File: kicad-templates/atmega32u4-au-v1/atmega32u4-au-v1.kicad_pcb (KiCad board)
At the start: 2 copper layers, 17 parts, among them P1 USB_C_Plug_USB2.0, U1 ATMEGA32U4-AU, U2 TPD2S017, Y1 16MHz

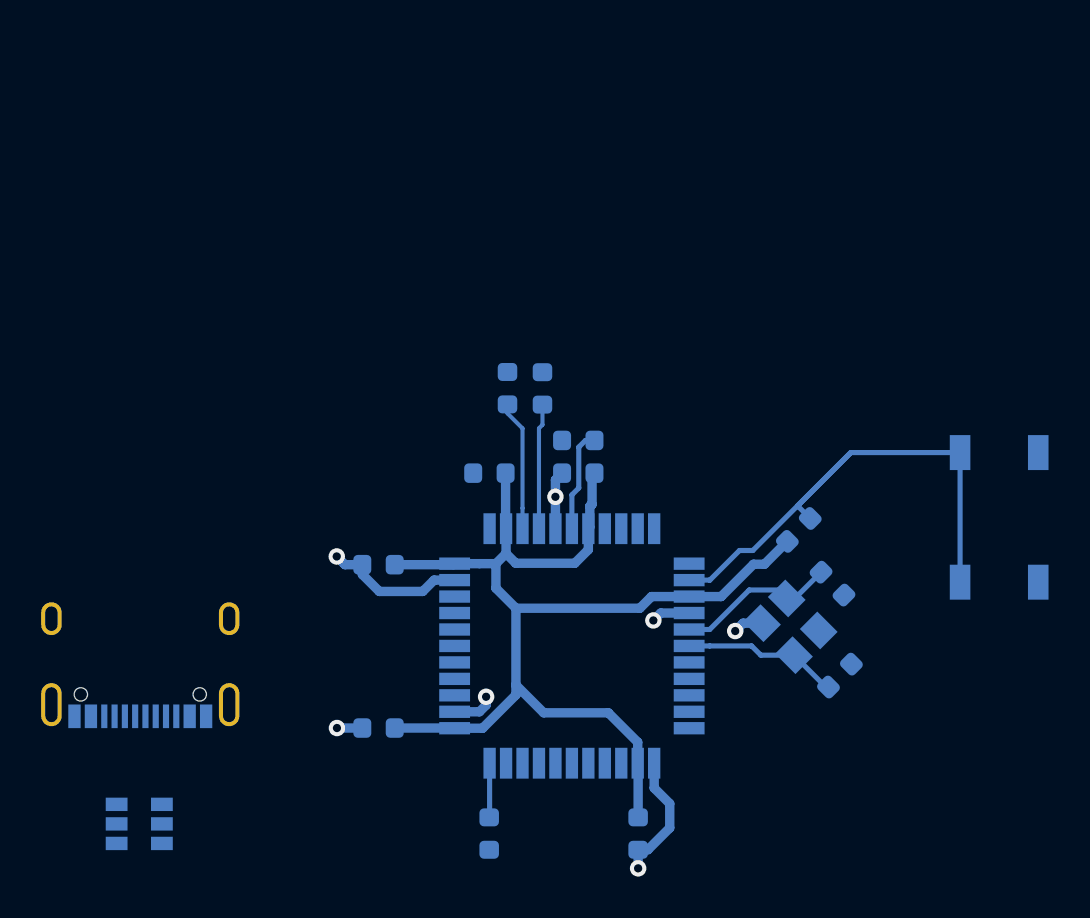
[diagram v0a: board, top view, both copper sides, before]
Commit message: change USB-C plug to receptacle, update template
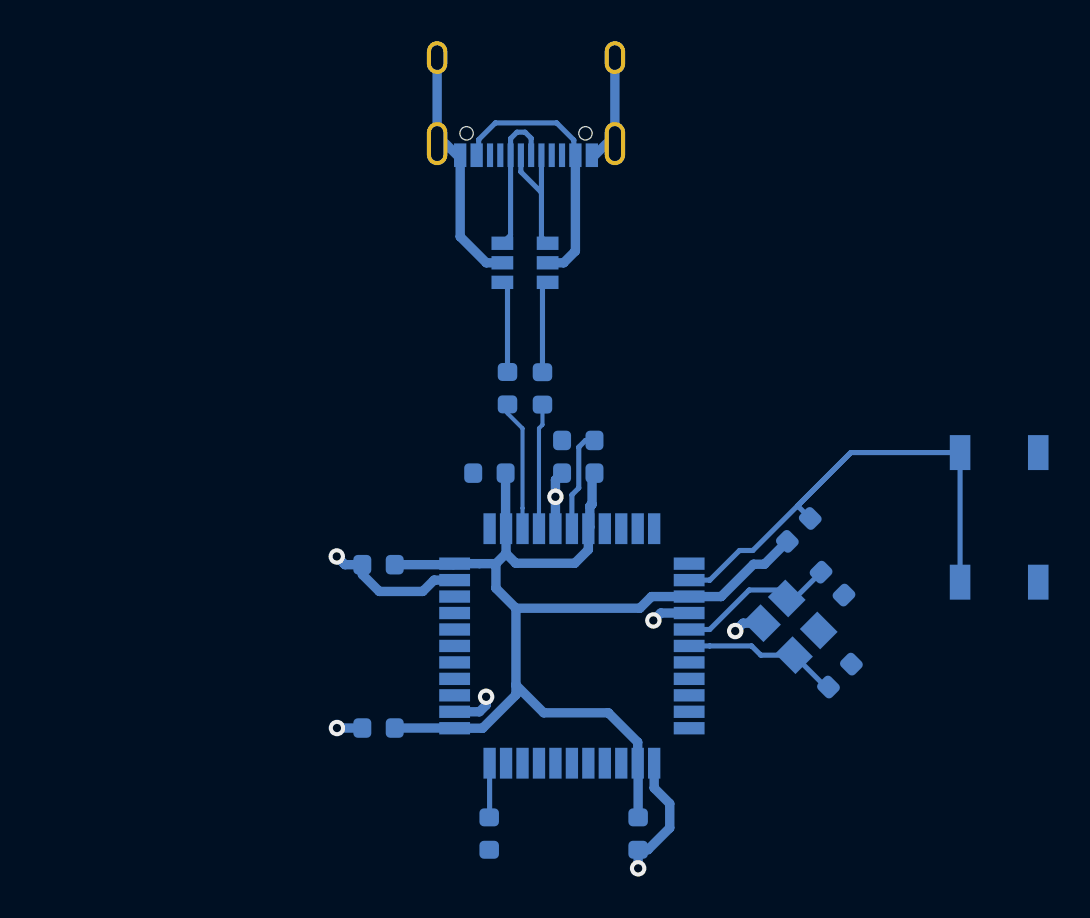
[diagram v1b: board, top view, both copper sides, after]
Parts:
- J1: renamed from P1; value USB_C_Plug_USB2.0 -> USB_C_Receptacle_USB2.0
- U1: value ATMEGA32U4-AU -> ATmega16U4-AU
- Y1: value 16MHz -> Crystal_GND24
- moved J1 33.1 mm to (18.8, -27.3)
- moved U2 33.1 mm to (18.7, -18.4)
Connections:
- C1 pad 1: (no net) -> N$1
- C1 pad 2: (no net) -> GND
- C2 pad 1: (no net) -> N$2
- C2 pad 2: (no net) -> GND
- C3 pad 1: (no net) -> VCC
- C3 pad 2: (no net) -> GND
- C4 pad 1: (no net) -> VCC
- C4 pad 2: (no net) -> GND
- C5 pad 1: (no net) -> VCC
- C5 pad 2: (no net) -> GND
- C6 pad 1: (no net) -> VCC
- C6 pad 2: (no net) -> GND
- C7 pad 1: (no net) -> VCC
- C7 pad 2: (no net) -> GND
- C8 pad 1: (no net) -> N$3
- C8 pad 2: (no net) -> GND
- J1 pad A1: (no net) -> GND
- J1 pad A12: (no net) -> GND
- J1 pad A4: (no net) -> VCC
- J1 pad A6: (no net) -> N$5
- J1 pad A7: (no net) -> N$4
- J1 pad A9: (no net) -> VCC
- J1 pad B1: (no net) -> GND
- J1 pad B12: (no net) -> GND
- J1 pad B4: (no net) -> VCC
- J1 pad B6: (no net) -> N$5
- J1 pad B7: (no net) -> N$4
- J1 pad B9: (no net) -> VCC
- J1 pad S1: (no net) -> GND
- R1 pad 1: (no net) -> N$8
- R1 pad 2: (no net) -> N$6
- R2 pad 1: (no net) -> N$9
- R2 pad 2: (no net) -> N$7
- R3 pad 1: (no net) -> N$10
- R3 pad 2: (no net) -> GND
- R4 pad 1: (no net) -> N$11
- R4 pad 2: (no net) -> VCC
- RST pad 1: (no net) -> GND
- RST pad 2: (no net) -> N$11
- U1 pad 13: (no net) -> N$11
- U1 pad 14: (no net) -> VCC
- U1 pad 15: (no net) -> GND
- U1 pad 16: (no net) -> N$2
- U1 pad 17: (no net) -> N$1
- U1 pad 2: (no net) -> VCC
- U1 pad 23: (no net) -> GND
- U1 pad 24: (no net) -> VCC
- U1 pad 3: (no net) -> N$8
- U1 pad 33: (no net) -> N$10
- U1 pad 34: (no net) -> VCC
- U1 pad 35: (no net) -> GND
- U1 pad 4: (no net) -> N$9
- U1 pad 43: (no net) -> GND
- U1 pad 44: (no net) -> VCC
- U1 pad 5: (no net) -> GND
- U1 pad 6: (no net) -> N$3
- U2 pad 1: (no net) -> N$6
- U2 pad 2: (no net) -> GND
- U2 pad 3: (no net) -> N$4
- U2 pad 4: (no net) -> N$5
- U2 pad 5: (no net) -> VCC
- U2 pad 6: (no net) -> N$7
- Y1 pad 1: (no net) -> N$1
- Y1 pad 2: (no net) -> GND
- Y1 pad 3: (no net) -> N$2
- Y1 pad 4: (no net) -> GND
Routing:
- net (no net): track 141.5 -> 0.07 mm, vias 7 -> 0
- net VCC: track 0.00 -> 69.2 mm
- net GND: track 0.00 -> 39.1 mm, vias 0 -> 7
- net N$11: track 0.00 -> 26.5 mm
- net N$2: track 0.00 -> 7.93 mm
- net N$1: track 0.00 -> 7.60 mm
- net N$4: track 0.00 -> 7.33 mm
- net N$5: track 0.00 -> 6.67 mm
- net N$8: track 0.00 -> 6.34 mm
- net N$9: track 0.00 -> 6.10 mm
- net N$3: track 0.00 -> 5.00 mm
- net N$7: track 0.00 -> 4.47 mm
- net N$6: track 0.00 -> 4.46 mm
- net N$10: track 0.00 -> 2.64 mm

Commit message: name nets in controller circuit, update template
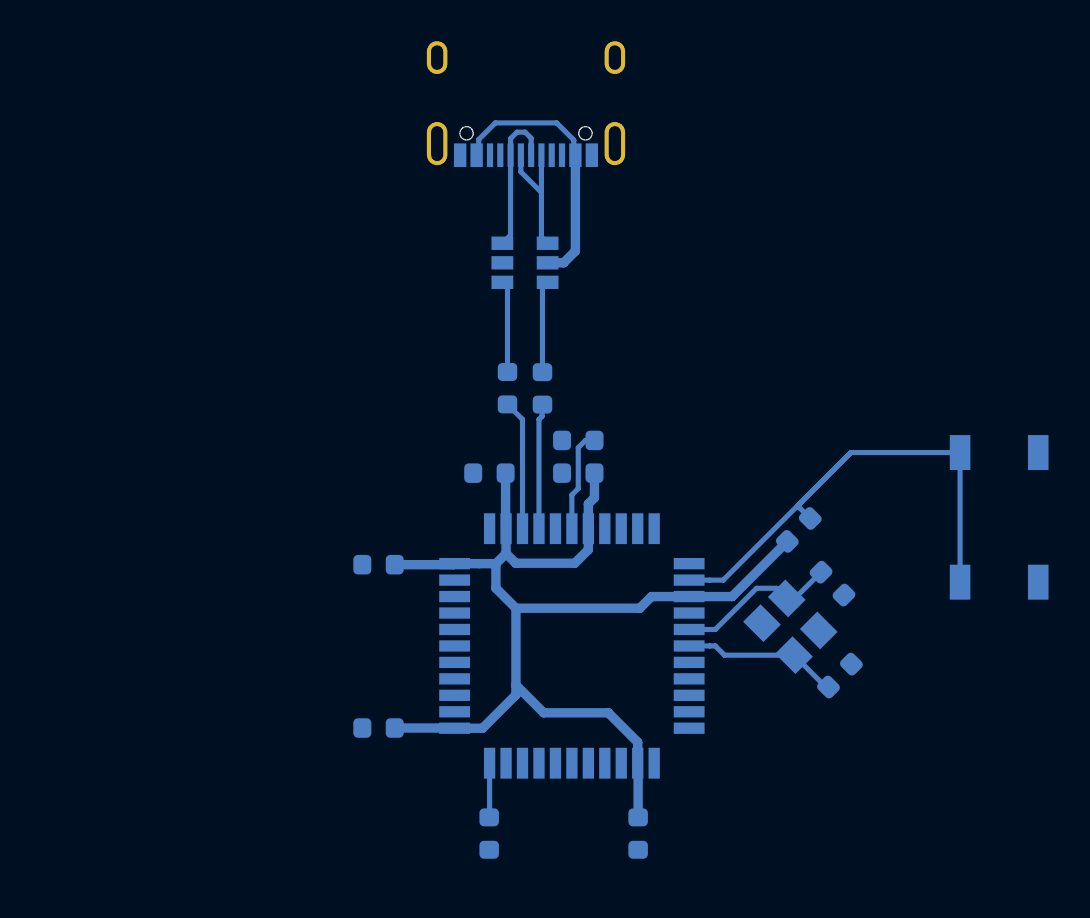
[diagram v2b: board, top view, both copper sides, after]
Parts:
- J1: footprint USB_C_Receptacle_XKB_U262-16XN-4BVC11 -> Connector_USB:USB_C_Receptacle_XKB_U262-16XN-4BVC11
- U1: footprint digikey-footprints:TQFP-44_10x10mm -> Package_QFP:TQFP-44_10x10mm_P0.8mm
- U2: footprint SOT-23-6 -> Package_TO_SOT_SMD:SOT-23-6
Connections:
- net N$1 renamed mcu/XTAL1
- net N$10 renamed mcu/~HWB~/PE2
- net N$11 renamed mcu/~RESET
- net N$2 renamed mcu/XTAL2
- net N$3 renamed mcu/UCAP
- net N$4 renamed usb/D-
- net N$5 renamed usb/D+
- net N$6 renamed u2/D-
- net N$7 renamed u2/D+
- net N$8 renamed mcu/D-
- net N$9 renamed mcu/D+
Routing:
- net GND: track 39.1 -> 0.00 mm, vias 7 -> 0

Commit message: Update to SKiDL 1.0.0 and use kicad v6 library
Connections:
- net mcu/~HWB~/PE2 renamed mcu/~{HWB}/PE2
- net mcu/~RESET renamed mcu/~{RESET}
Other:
- net class Default removed
